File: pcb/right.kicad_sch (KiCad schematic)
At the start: 118 parts, among them Q201 AO3401A, Q202 AO3401A, Q203 AO3400A, SW201 -, SW202 0, SW203 9, SW204 8, SW205 7, SW206 6, SW208 \, SW209 P, SW210 O, SW211 I, SW212 U, SW213 Y, SW214 ', SW215 ;, SW216 L, SW217 K, SW218 J, SW219 H, SW220 Alt, SW221 Shift, SW222 /, SW223 ., SW224 ,, SW225 M, SW226 N, SW227 Ctrl, SW228 ], SW229 [, SW230 Down, SW231 Up, SW232 Fn, SW233 Space, SW234 Enter, SW290 MSK12C02 power, SW291 Reset, U201 nRF52840 Pro Micro

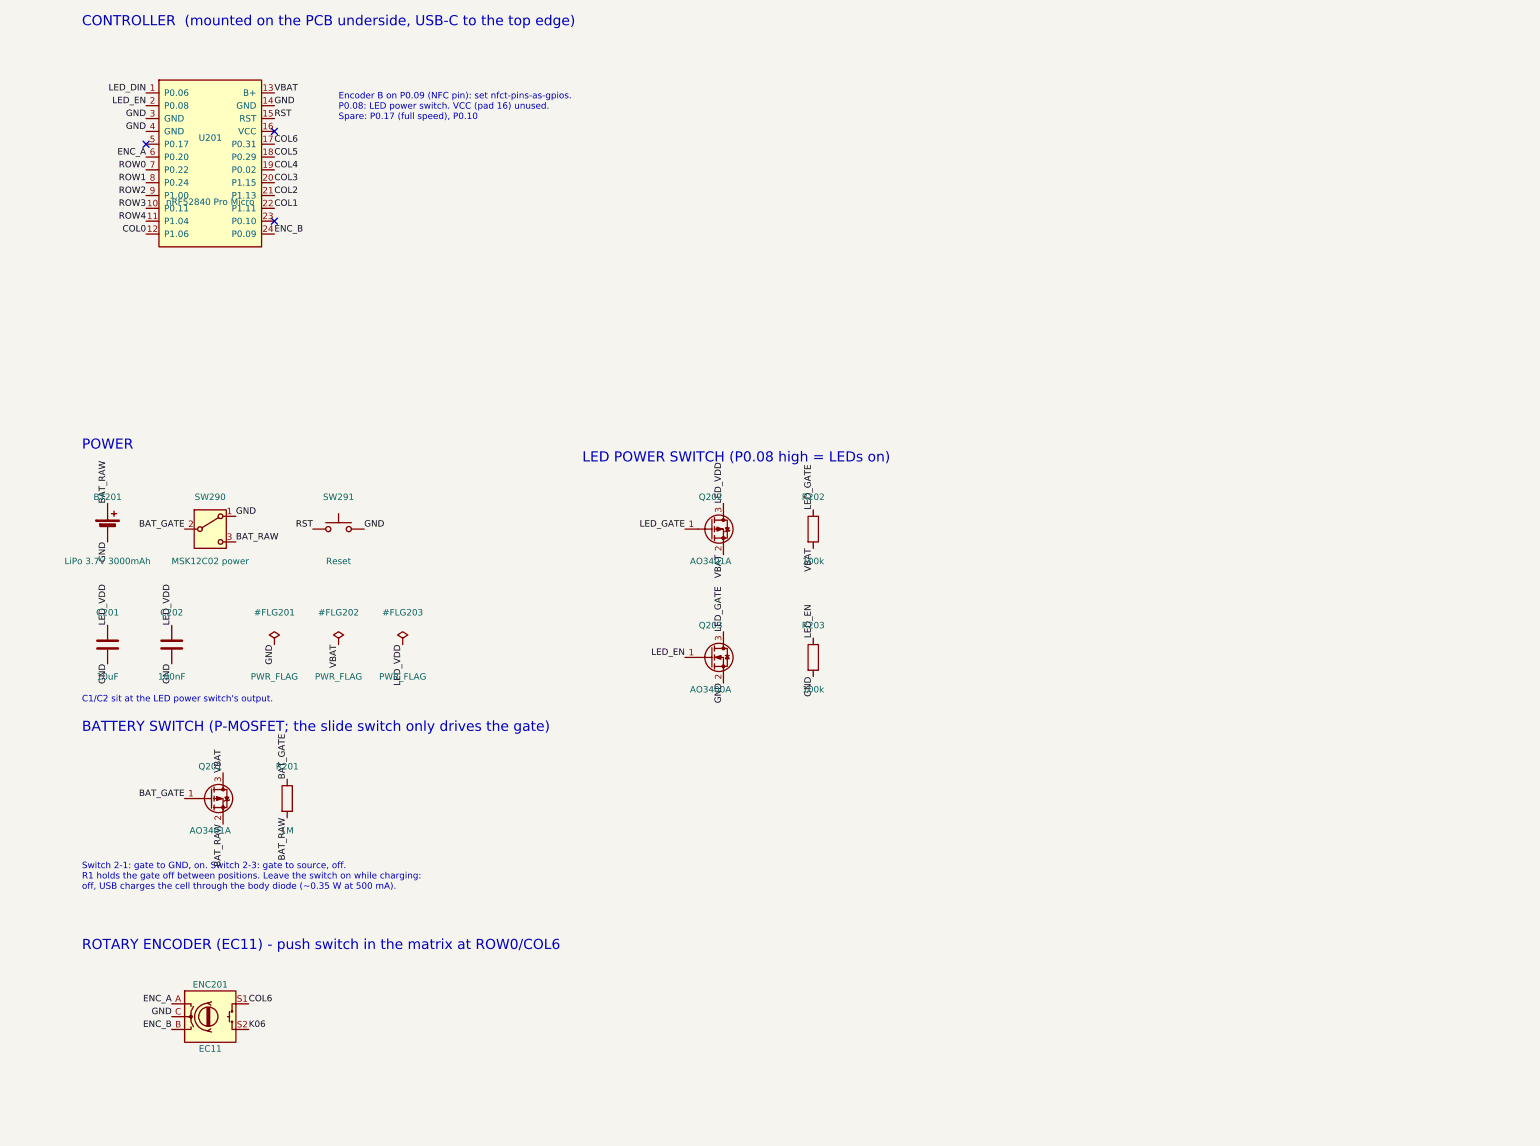
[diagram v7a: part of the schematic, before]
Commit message: Add the switch plate, the gasket-mounted case, two OLEDs and a second knob
Switch plate: a 1.6 mm FR-4 board with black mask and no copper, made by
the PCB fab. tools/gen_plate.py writes it as its own KiCad board
(pcb/plate/) with Gerbers per half and fab/PLATE.md. It follows the PCB
outline with eight gasket tabs per half, 14 mm switch cut-outs, an
encoder cut-out and an OLED window per half, and the M2 holes.

Case: a 3D-printed PETG bottom shell and top frame per half, written by
tools/gen_case.py (build123d) to case/ as STL and STEP. The plate and
PCB, tied by M2 standoffs, float on Poron strips above and below each
tab; eight M2 screws per half close the case into heat-set inserts. It
has an open USB-C slot, a power switch slot with the wall thinned in
front, and a guided reset pinhole. A fit check against the PCB, plate,
controller, reset button, OLEDs and keycaps at full travel finds no
overlaps. The floor stays flat until tenting is chosen. Shared geometry
is in tools/case_geometry.py; tools/render_case.py renders the case and
the plate.

Knobs and OLEDs: the right encoder moves 7.6 mm inward and 4.1 mm up,
from 0.5 mm to 8.1 mm clear of the nearest keycap, and a mirrored
encoder joins the left half (push at row 0 / column 6, which renumbers
the left keys after it to SW108-SW134 / D108-D134). Each half gets a
0.96 in. SSD1306 OLED (J101/J201) over the controller's lower end, on
P0.17/P0.20, powered from the nice!nano's switched VCC. Both encoders
move to P0.10/P0.09, so both halves share one pin map with every edge
pin in use. The left reset button moves 6.5 mm so both halves mirror.
The new parts were added to the routed board and rerouted locally with
finish_route.py and smooth_route.py; the artwork was redrawn.

Firmware: both encoders, ZMK's status screen on both OLEDs (blanking
when idle), P0.13 held high by a gpio-hog for the OLED's power, and
ext-power on P0.08 only. The left knob scrolls (Super + scroll walks
Hyprland's workspaces) and clicks the mid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
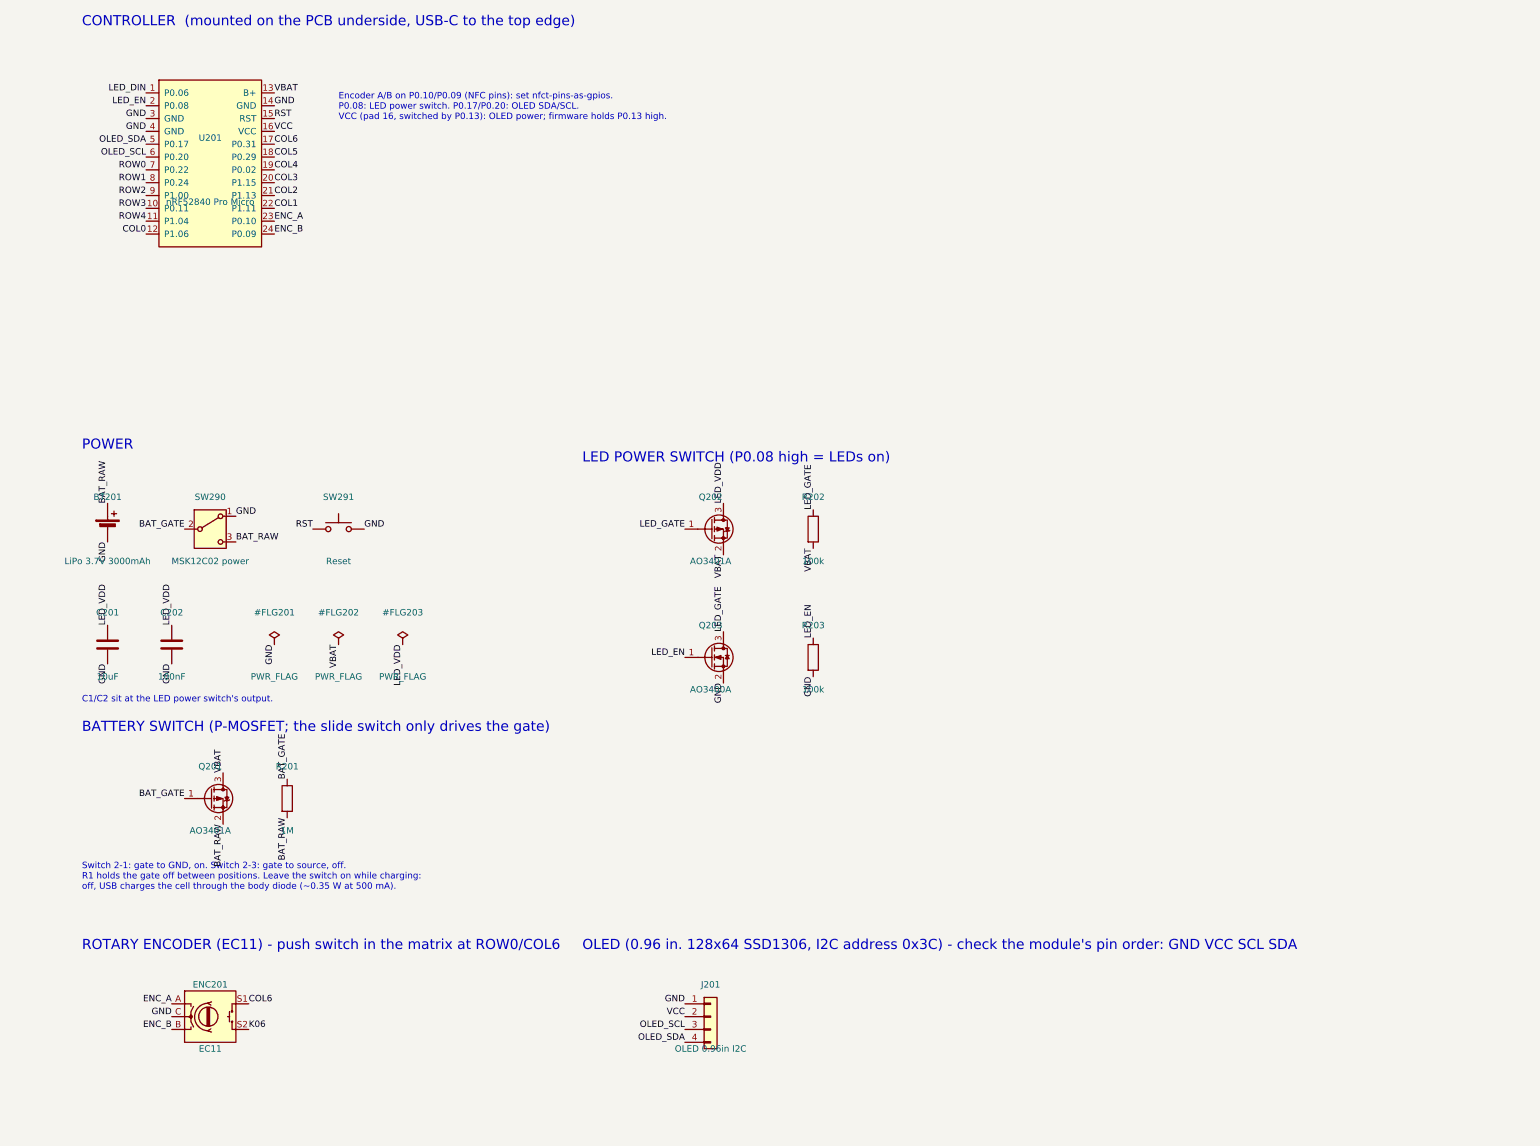
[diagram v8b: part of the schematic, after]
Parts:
- added J201: OLED 0.96in I2C, Connector_PinHeader_2.54mm:PinHeader_1x04_P2.54mm_Vertical, symbol Connector_Generic:Conn_01x04
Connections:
- net ENC_A: now also U201.23 (P0.10); no longer U201.6 (P0.20)
- net GND: now also J201.1 (Pin_1)
- net VCC: now reaches U201.16 (VCC)
- net VCC: now also J201.2 (Pin_2)
- net OLED_SDA: now reaches U201.5 (P0.17)
- net OLED_SDA: now also J201.4 (Pin_4)
- new net OLED_SCL: J201.3 (Pin_3), U201.6 (P0.20)
- no-connect marks 4 -> 1
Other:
- note added: "Encoder A/B on P0.10/P0.09 (NFC pins): set nfct-pins-as-gpios. P0.08: LED power switch. P0.17/P0.20: OLED SDA/SCL. VCC (pad 16, switched by P0.13): OLED power; firmware holds P0.13 high."
- note added: "OLED (0.96 in. 128x64 SSD1306, I2C address 0x3C) - check the module's pin order: GND VCC SCL SDA"
- note removed: "Encoder B on P0.09 (NFC pin): set nfct-pins-as-gpios. P0.08: LED power switch. VCC (pad 16) unused. Spare: P0.17 (full speed), P0.10"
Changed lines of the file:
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@@
     (effects (font (size 1.27 1.27)) (justify right bottom))
   )
-  (no_connect (at 347.98 55.88))
-  (label "ENC_A"
+  (label "OLED_SDA"
+    (at 347.98 55.88 180)
+    (effects (font (size 1.27 1.27)) (justify right bottom))
+  )
+  (label "OLED_SCL"
     (at 347.98 58.42 180)
     (effects (font (size 1.27 1.27)) (justify right bottom))
@@
     (effects (font (size 1.27 1.27)) (justify left bottom))
   )
-  (no_connect (at 373.38 53.34))
+  (label "VCC"
+    (at 373.38 53.34 0)
+    (effects (font (size 1.27 1.27)) (justify left bottom))
+  )
   (label "COL6"
     (at 373.38 55.88 0)
@@
     (effects (font (size 1.27 1.27)) (justify left bottom))
   )
-  (no_connect (at 373.38 71.12))
+  (label "ENC_A"
+    (at 373.38 71.12 0)
+    (effects (font (size 1.27 1.27)) (justify left bottom))
+  )
   (label "ENC_B"
     (at 373.38 73.66 0)
     (effects (font (size 1.27 1.27)) (justify left bottom))
   )
-  (text "Encoder B on P0.09 (NFC pin): set nfct-pins-as-gpios.\nP0.08: LED power switch. VCC (pad 16) unused.\nSpare: P0.17 (full speed), P0.10"
+  (text "Encoder A/B on P0.10/P0.09 (NFC pins): set nfct-pins-as-gpios.\nP0.08: LED power switch. P0.17/P0.20: OLED SDA/SCL.\nVCC (pad 16, switched by P0.13): OLED power; firmware holds P0.13 high."
     (exclude_from_sim no)
     (at 386.08 45.72 0)
@@
     (effects (font (size 1.27 1.27)) (justify left bottom))
   )
+  (text "OLED (0.96 in. 128x64 SSD1306, I2C address 0x3C) - check the module's pin order: GND VCC SCL SDA"
+    (exclude_from_sim no)
+    (at 434.34 213.36 0)
+    (effects (font (size 2 2)) (justify left top))
+  )
+  (symbol
+    (lib_id "Connector_Generic:Conn_01x04")
+    (at 459.74 228.6 0)
+    (unit 1)
+    (exclude_from_sim no)
+    (in_bom yes)
+    (on_board yes)
+    (dnp no)
+    (property "Reference" "J201" (at 459.74 222.25 0) (effects (font (size 1.27 1.27))))
+    (property "Value" "OLED 0.96in I2C" (at 459.74 234.95 0) (effects (font (size 1.27 1.27))))
+    (property "Footprint" "Connector_PinHeader_2.54mm:PinHeader_1x04_P2.54mm_Vertical"
+      (at 459.74 228.6 0)
+      (effects (font (size 1.27 1.27)) (hide yes))
+    )
+    (property "Datasheet" "" (at 459.74 228.6 0) (effects (font (size 1.27 1.27)) (hide yes)))
+    (pin "1")
+    (pin "2")
+    (pin "3")
+    (pin "4")
+    (instances
+      (project "keygen"
+        (path "/6967da33-a0e5-5fa7-9742-40725aff3c90/0c428d53-712b-56dc-b044-5fe085247794"
+          (reference "J201")
+          (unit 1)
+        )
+      )
+    )
+  )
+  (label "GND"
+    (at 454.66 226.06 180)
+    (effects (font (size 1.27 1.27)) (justify right bottom))
+  )
+  (label "VCC"
+    (at 454.66 228.6 180)
+    (effects (font (size 1.27 1.27)) (justify right bottom))
+  )
+  (label "OLED_SCL"
+    (at 454.66 231.14 180)
+    (effects (font (size 1.27 1.27)) (justify right bottom))
+  )
+  (label "OLED_SDA"
+    (at 454.66 233.68 180)
+    (effects (font (size 1.27 1.27)) (justify right bottom))
+  )
   (text "MOUNTING HOLES (M2)"
